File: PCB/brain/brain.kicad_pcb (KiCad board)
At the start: 2 copper layers, 217 parts, among them J1 Screw_Terminal_01x02, J10 Conn_01x12, J11 Conn_01x04, J12 BAT, J2 Conn_01x04, J3 RJ45_Hanrun_HR911105A_Horizon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, J4 Conn_01x04, J5 Conn_01x04, J6 Conn_01x04, J7 Conn_01x06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

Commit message: start pcb routing
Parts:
- moved R51 445.0 mm to (-243.4, 328.6)
- moved R56 439.2 mm to (-242.8, 332.0), turned to -90 degrees
- moved R57 439.0 mm to (-244.3, 332.0), turned to -90 degrees
- moved C84 423.7 mm to (-243.4, 327.0), turned to 180 degrees
- moved J10 422.9 mm to (-324.7, 245.8)
- moved RV1 419.0 mm to (-237.5, 328.7), turned to -90 degrees
- moved C87 416.0 mm to (-238.8, 325.2), turned to -135 degrees
- moved JP3 413.6 mm to (-249.5, 329.7), turned to 90 degrees
- moved R46 412.3 mm to (-208.3, 308.4)
- moved R47 412.3 mm to (-208.3, 311.0)
- moved R48 412.3 mm to (-208.3, 313.5)
- moved R49 412.3 mm to (-208.3, 316.0)
- moved R50 412.3 mm to (-208.3, 318.5)
- moved C88 411.9 mm to (-235.8, 324.8), turned to 90 degrees
- moved JP2 411.0 mm to (-260.0, 321.3), turned to 180 degrees
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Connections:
- C16 pad 2: PMODE0 -> +3.3V
- C57 pad 2: PMODE0 -> +3.3V
- C58 pad 2: PMODE0 -> +3.3V
- C61 pad 2: PMODE0 -> +3.3V
- C62 pad 2: PMODE0 -> +3.3V
- C8 pad 2: PMODE0 -> +3.3V
- C81 pad 2: PMODE0 -> +3.3V
- C82 pad 2: PMODE0 -> +3.3V
- C87 pad 1: PMODE0 -> +3.3V
- C88 pad 2: PMODE0 -> +3.3V
- C89 pad 2: PMODE0 -> +3.3V
- D3 pad 2: PMODE0 -> +3.3V
- FB3 pad 1: PMODE0 -> +3.3V
- J10 pad 4: PMODE0 -> +3.3V
- J3 pad 12: PMODE0 -> +3.3V
- J3 pad 9: PMODE0 -> +3.3V
- J8 pad 2: PMODE0 -> +3.3V
- J8 pad 3: PMODE0 -> +3.3V
- J9 pad 1: OA1 -> OA2
- J9 pad 2: OA2 -> OA1
- JP1 pad 1: PMODE0 -> +3.3V
- JP3 pad 1: PMODE0 -> +3.3V
- JP4 pad 1: PMODE0 -> +3.3V
- L4 pad 2: PMODE0 -> +3.3V
- R12 pad 2: PMODE0 -> +3.3V
- R13 pad 2: PMODE0 -> +3.3V
- R25 pad 1: PMODE0 -> +3.3V
- R29 pad 2: PMODE0 -> +3.3V
- R4 pad 1: PMODE0 -> +3.3V
- R48 pad 1: PMODE0 -> +3.3V
- R52 pad 1: PMODE0 -> +3.3V
- R53 pad 1: PMODE0 -> +3.3V
- R54 pad 1: PMODE0 -> +3.3V
- R55 pad 1: PMODE0 -> +3.3V
- U1 pad 2: PMODE0 -> +3.3V
- U10 pad 3: PMODE0 -> +3.3V
- U14 pad 1: PMODE0 -> +3.3V
- U2 pad 15: PMODE0 -> +3.3V
- U3 pad 28: PMODE0 -> +3.3V
- U3 pad 43: PMODE0 -> PMODE2
- U3 pad 44: PMODE0 -> PMODE1
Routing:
- net GND: track 0.00 -> 112.1 mm, vias 0 -> 7
- net Net-(BT1--): track 0.00 -> 40.2 mm, vias 0 -> 1
- net VS: track 0.00 -> 35.6 mm, vias 0 -> 3
- net +3.3V: track 0.00 -> 34.2 mm, vias 0 -> 4
- net +5V: track 0.00 -> 25.6 mm, vias 0 -> 2
- net +BATT: track 0.00 -> 23.5 mm
- net Net-(BT2--): track 0.00 -> 22.3 mm
- net OA2: track 0.00 -> 12.6 mm
- net OB2: track 0.00 -> 12.6 mm
- net OB1: track 0.00 -> 11.4 mm
- net OA1: track 0.00 -> 11.4 mm
- net Net-(Q1-D): track 0.00 -> 8.29 mm, vias 0 -> 19
- net Net-(Q1-G): track 0.00 -> 8.29 mm, vias 0 -> 2
- net MS1: track 0.00 -> 7.01 mm
- net MS2: track 0.00 -> 6.67 mm, vias 0 -> 2
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
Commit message: TMC2209 done
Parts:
- moved J10 113.9 mm to (-256.6, 337.0), turned to 90 degrees
- moved D11 55.2 mm to (-233.8, 315.8), turned to 180 degrees
- moved D10 49.1 mm to (-236.8, 319.0), turned to 180 degrees
- moved D9 48.1 mm to (-236.8, 317.4)
- moved R46 43.6 mm to (-249.8, 321.6), turned to -90 degrees
- moved C85 40.4 mm to (-258.0, 319.6), turned to -90 degrees
- moved C80 37.5 mm to (-256.5, 319.6), turned to -90 degrees
- moved R47 28.7 mm to (-236.8, 314.2), turned to 180 degrees
- moved R50 28.7 mm to (-236.8, 315.8), turned to 180 degrees
- moved C79 28.5 mm to (-246.8, 322.4), turned to -90 degrees
- moved C83 28.1 mm to (-247.2, 325.0)
- moved R48 25.8 mm to (-233.8, 317.4), turned to 180 degrees
- moved R49 25.5 mm to (-233.6, 319.0)
- moved JP2 1.40 mm to (-261.4, 321.3)
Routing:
- net GND: track 112.1 -> 142.1 mm, vias 7 -> 9
- net STEP: track 1.42 -> 11.9 mm, vias 1 -> 2
- net VS: track 35.6 -> 44.8 mm
- net +3.3V: track 34.2 -> 42.0 mm
- net Net-(JP3-B): track 0.00 -> 7.56 mm
- net DIR: track 0.00 -> 5.60 mm
- net EN: track 0.00 -> 5.52 mm, vias 0 -> 2
- net VCP: track 0.00 -> 2.61 mm
- net Net-(U2-CPO): track 0.00 -> 1.99 mm
- net Net-(U2-CPI): track 0.00 -> 1.95 mm
- net Net-(D10-K): track 0.00 -> 1.59 mm
- net Net-(D9-A): track 0.00 -> 1.39 mm
- net Net-(D11-A): track 0.00 -> 1.39 mm

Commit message: more pcb routing
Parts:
- added C94: 22uF, Capacitor_SMD:C_0805_2012Metric, F.Cu at (-47.9, 179.5)
- C25, C28, C36, C40, C59, C62, C64, C65, C66, C67, C68, C69, C8, C82, C9: footprint Capacitor_SMD:C_0603_1608Metric -> Capacitor_SMD:C_0402_1005Metric
- U11: footprint easyeda2kicad:SOIC-8_L4.9-W3.9-P1.27-LS6.0-BL-EP-1 -> Package_SO:SOIC-8-1EP_3.9x4.9mm_P1.27mm_EP2.29x3mm_ThermalVias
- moved R59 414.3 mm to (-44.9, 182.0), turned to 180 degrees
- moved U11 410.6 mm to (-38.2, 181.1)
- moved R41 408.9 mm to (-37.8, 163.2)
- moved R40 405.2 mm to (-34.7, 163.2)
- moved R26 395.5 mm to (-32.7, 181.9)
- moved R28 394.7 mm to (-36.9, 185.1), turned to 180 degrees
- moved R27 391.2 mm to (-33.8, 185.1), turned to 180 degrees
- moved C53 390.7 mm to (-43.1, 179.7), turned to -90 degrees
- moved L2 389.3 mm to (-30.2, 172.6), turned to 90 degrees
- moved C48 389.1 mm to (-37.8, 171.6)
- moved C43 388.8 mm to (-37.8, 169.5)
- moved C54 388.5 mm to (-46.1, 179.7), turned to -90 degrees
- moved C42 388.4 mm to (-37.8, 167.4)
- moved C41 387.5 mm to (-44.6, 179.7), turned to -90 degrees
- moved C47 386.7 mm to (-40.5, 177.5), turned to 180 degrees
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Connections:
- net Net-(U9-SW1) renamed /SW1
- net Net-(U9-SW2) renamed /SW2
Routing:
- net GND: track 142.1 -> 235.3 mm
- net 5VHP: track 0.00 -> 38.0 mm, vias 0 -> 2
- net Net-(U11-SW): track 0.00 -> 16.6 mm, vias 0 -> 2
- net AMP_VDD: track 0.00 -> 15.3 mm
- net Net-(C6-Pad1): track 0.00 -> 8.64 mm
- net Net-(C5-Pad1): track 0.00 -> 8.64 mm
- net VSYS: track 4.92 -> 12.9 mm
- net Net-(U11-COMP): track 0.00 -> 4.53 mm
- net 5VHP_EN: track 0.00 -> 3.22 mm, vias 0 -> 1
- net Net-(U4-OUTP): track 0.00 -> 2.92 mm
- net Net-(U4-OUTN): track 0.00 -> 2.92 mm
- net Net-(U11-FB): track 0.00 -> 2.25 mm
- net Net-(U11-SS): track 0.00 -> 2.23 mm
- net Net-(U4-~{SD_MODE}): track 0.00 -> 1.80 mm
- net Net-(U11-BST): track 0.00 -> 1.70 mm
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- added copper zone on F.Cu, net /SW1
- added copper zone on F.Cu, net /SW2

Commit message: start component placing on pcb
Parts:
- added C95: 10uF, Capacitor_SMD:C_0603_1608Metric, F.Cu at (257.5, 75.0)
- added C96: 0.1uF, Capacitor_SMD:C_0402_1005Metric, F.Cu at (257.2, 76.5)
- added MK1: ICS-43434, Sensor_Audio:InvenSense_ICS-43434-6_3.5x2.65mm, F.Cu at (254.5, 77.9)
- C30, C31, C32: moved to B.Cu
- moved BT1 243.4 mm to (61.8, 52.8), turned to -90 degrees
- moved BT2 240.5 mm to (55.3, 52.8), turned to -90 degrees
- moved J12 233.6 mm to (54.8, 57.8), turned to 0 degrees
- moved C2 227.8 mm to (57.5, 63.0), turned to 180 degrees
- moved C15 227.7 mm to (67.1, 66.8), turned to 0 degrees
- moved C1 226.1 mm to (58.3, 64.6), turned to 180 degrees
- moved R15 224.3 mm to (59.0, 66.2), turned to 180 degrees
- moved U10 223.8 mm to (67.1, 69.8), turned to 180 degrees
- moved R29 222.7 mm to (65.1, 69.8), turned to 90 degrees
- moved R14 221.7 mm to (58.2, 67.8), turned to 0 degrees
- moved U7 218.1 mm to (58.1, 70.5), turned to 0 degrees
- moved R7 216.7 mm to (60.6, 72.5), turned to -90 degrees
- moved C3 214.2 mm to (55.6, 72.5), turned to 90 degrees
- moved Q2 211.2 mm to (60.2, 76.6), turned to -90 degrees
- moved Q1 209.0 mm to (56.1, 76.6), turned to -90 degrees
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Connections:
- net Net-(U9-PMID) renamed /PMID
- C37 pad 2: VSYS -> VBUS
- C38 pad 2: VSYS -> VBUS
- C39 pad 2: VSYS -> VBUS
- C40 pad 2: VSYS -> VBUS
- R25 pad 2: INT -> BQINT
- TP6 pad 1: INT -> BQINT
- U1 pad 24: unconnected-(U1-IO47-Pad24) -> MicDATA
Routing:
- net GND: track 235.3 -> 355.4 mm, vias 9 -> 90
- net VBUS: track 0.00 -> 37.5 mm
- net Net-(BT1--): track 40.2 -> 10.0 mm
- net VSYS: track 12.9 -> 40.5 mm, vias 0 -> 7
- net REGN: track 0.00 -> 20.7 mm, vias 0 -> 4
- net Net-(R1-Pad1): track 0.00 -> 19.3 mm
- net D-: track 0.00 -> 15.7 mm
- net +3.3V: track 42.0 -> 57.1 mm, vias 4 -> 6
- net SDA: track 0.00 -> 15.0 mm, vias 0 -> 3
- net SCL: track 0.00 -> 14.7 mm, vias 0 -> 3
- net D+: track 0.00 -> 14.3 mm
- net CC1: track 0.00 -> 13.2 mm
- net BQINT: track 0.00 -> 12.9 mm
- net /PMID: track 0.00 -> 12.8 mm
- net CC2: track 0.00 -> 12.3 mm
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- added copper zone on B.Cu, net +BATT
- added copper zone on F.Cu, net +BATT
- added copper zone on F.Cu, net 5VHP
- added copper zone on F.Cu, net 5VHP_EN
- added copper zone on B.Cu, net GND
- added copper zone on F.Cu, net GND
- added copper zone on B.Cu, net Net-(BT1--)
- added copper zone on B.Cu, net Net-(BT2--)
- added copper zone on F.Cu, net Net-(BT2--)
- added copper zone on F.Cu, net Net-(U11-BST)
- added copper zone on F.Cu, net Net-(U11-FB)
- added copper zone on F.Cu, net Net-(U11-SW)
- added copper zone on B.Cu, net REGN
- added copper zone on F.Cu, net VBUS
- added copper zone on F.Cu, net VSYS
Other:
- board outline added: 100 x 100 mm

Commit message: more pcb
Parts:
- J10: footprint Connector_PinSocket_2.54mm:PinSocket_1x12_P2.54mm_Vertical -> Connector_PinHeader_2.54mm:PinHeader_2x06_P2.54mm_Vertical
- moved JP2 287.9 mm to (101.5, 77.2), turned to 0 degrees
- moved C85 271.4 mm to (88.8, 80.3), turned to 180 degrees
- moved C80 269.4 mm to (88.8, 81.8), turned to 180 degrees
- moved C86 269.1 mm to (94.9, 82.6), turned to 0 degrees
- moved R46 263.5 mm to (89.5, 85.0), turned to 180 degrees
- moved J9 260.1 mm to (102.5, 92.2), turned to 90 degrees
- moved JP3 259.9 mm to (81.4, 85.3), turned to 0 degrees
- moved C79 259.1 mm to (88.7, 88.0), turned to 180 degrees
- moved R45 259.1 mm to (95.0, 90.1), turned to 0 degrees
- moved J10 258.9 mm to (67.3, 82.7), turned to 0 degrees
- moved C83 258.6 mm to (86.1, 87.6), turned to -90 degrees
- moved U2 253.6 mm to (88.9, 92.2), turned to -90 degrees
- moved R44 253.4 mm to (95.0, 94.4), turned to 0 degrees
- moved C84 252.6 mm to (84.1, 91.4), turned to 90 degrees
- moved R51 252.0 mm to (82.5, 91.4), turned to -90 degrees
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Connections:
- J10 pad 10: EN -> TmcEN
- R46 pad 1: EN -> TmcEN
- U1 pad 11: EN -> TmcEN
- U2 pad 2: EN -> TmcEN
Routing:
- net +3.3V: track 57.1 -> 80.4 mm, vias 6 -> 22
- net VS: track 44.8 -> 27.8 mm, vias 3 -> 2
- net TmcEN: track 0.00 -> 7.50 mm, vias 0 -> 3
- net EN: track 17.1 -> 11.6 mm, vias 2 -> 0
- net GND: track 355.4 -> 351.3 mm, vias 90 -> 134
- net SDA: track 15.0 -> 18.2 mm
- net RX1: track 0.00 -> 2.31 mm, vias 0 -> 1
- net BQINT: track 12.9 -> 15.0 mm, vias 0 -> 1
- net STEP: track 11.9 -> 13.9 mm, vias 2 -> 3
- net RSTn: track 0.00 -> 1.98 mm, vias 0 -> 1
- net DIR: track 5.60 -> 7.57 mm, vias 0 -> 1
- net CE: track 10.5 -> 12.4 mm, vias 2 -> 3
- net TX1: track 0.00 -> 1.88 mm, vias 0 -> 1
- net SCL: track 14.7 -> 16.6 mm
- net +5V: vias 2 -> 15
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- added copper zone on B.Cu, net +3.3V
- added copper zone on F.Cu, net +3.3V
- added copper zone on B.Cu, net +5V
- added copper zone on F.Cu, net +5V
- added copper zone on F.Cu, net OB2
- added copper zone on B.Cu, net VBUS
- added copper zone on F.Cu, net VS
- added copper zone on B.Cu, net VSYS
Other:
- outline, holes or cut-outs redrawn

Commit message: more pcb
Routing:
- net DIR: track 7.57 -> 52.6 mm, vias 1 -> 2
- net TmcEN: track 7.50 -> 41.8 mm, vias 3 -> 4
- net STEP: track 13.9 -> 46.8 mm
- net DIAG: track 1.74 -> 25.7 mm, vias 1 -> 2
- net VS: track 27.8 -> 47.5 mm, vias 2 -> 3
- net UART: track 2.84 -> 21.2 mm, vias 1 -> 2
- net INDEX: track 4.10 -> 21.6 mm, vias 1 -> 2
- net MS2: track 6.67 -> 20.7 mm
- net +3.3V: track 80.4 -> 91.3 mm
- net MS1: track 7.01 -> 17.9 mm
- net GND: track 351.3 -> 352.6 mm, vias 134 -> 135
- added copper zone on F.Cu, net OA1
- added copper zone on F.Cu, net OA2
- added copper zone on F.Cu, net OB1

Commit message: moar pcb
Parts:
- added J13: Conn_01x05, Connector_JST:JST_XH_B5B-XH-A_1x05_P2.50mm_Vertical, F.Cu at (53.5, 99.0)
- added J14: Conn_01x02, Connector_PinSocket_2.54mm:PinSocket_1x02_P2.54mm_Vertical, F.Cu at (84.0, 110.0)
- moved C95 199.2 mm to (58.9, 91.0), turned to 90 degrees
- moved C96 197.4 mm to (60.4, 91.3), turned to 90 degrees
- moved MK1 193.3 mm to (61.9, 94.0), turned to 90 degrees
- moved LS1 159.4 mm to (115.6, 92.5), turned to 0 degrees
- moved JP1 154.7 mm to (109.6, 76.3), turned to 0 degrees
- moved C6 154.3 mm to (115.3, 85.8), turned to 180 degrees
- moved C60 152.1 mm to (112.6, 78.1), turned to 90 degrees
- moved FB1 151.5 mm to (116.1, 83.3), turned to -90 degrees
- moved C5 150.8 mm to (118.3, 85.8), turned to 0 degrees
- moved C59 150.3 mm to (114.1, 78.1), turned to 90 degrees
- moved FB2 149.7 mm to (117.6, 83.3), turned to -90 degrees
- moved U4 146.5 mm to (117.3, 78.4), turned to -90 degrees
- moved R30 144.6 mm to (116.6, 74.3), turned to 90 degrees
- moved C10 104.4 mm to (102.5, 43.0), turned to -90 degrees
- moved J2 95.6 mm to (109.0, 46.8), turned to 90 degrees
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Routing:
- net GND: track 352.6 -> 371.2 mm, vias 135 -> 151
- net BCLK: track 0.00 -> 11.8 mm
- net LRCLK: track 0.00 -> 7.69 mm
- net MicDATA: track 0.00 -> 7.02 mm
- net AMP_VDD: track 15.3 -> 21.0 mm
- net RX0: track 0.00 -> 5.55 mm
- net TX0: track 0.00 -> 5.48 mm
- net Net-(J11-Pin_1): track 0.00 -> 5.26 mm
- net +3.3V: track 91.3 -> 92.6 mm, vias 22 -> 24
- net VSYS: vias 17 -> 26
- net +5V: vias 15 -> 23
- net (no net): vias 0 -> 1
- added copper zone on F.Cu, net AMP_VDD
- added copper zone on F.Cu, net Net-(C5-Pad1)
- added copper zone on F.Cu, net Net-(C6-Pad1)
- added copper zone on F.Cu, net Net-(U4-OUTN)
- added copper zone on F.Cu, net Net-(U4-OUTP)
- added copper zone on B.Cu, net SCL
- added copper zone on B.Cu, net SDA
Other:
- board size 100 x 100 mm -> 100 x 115 mm

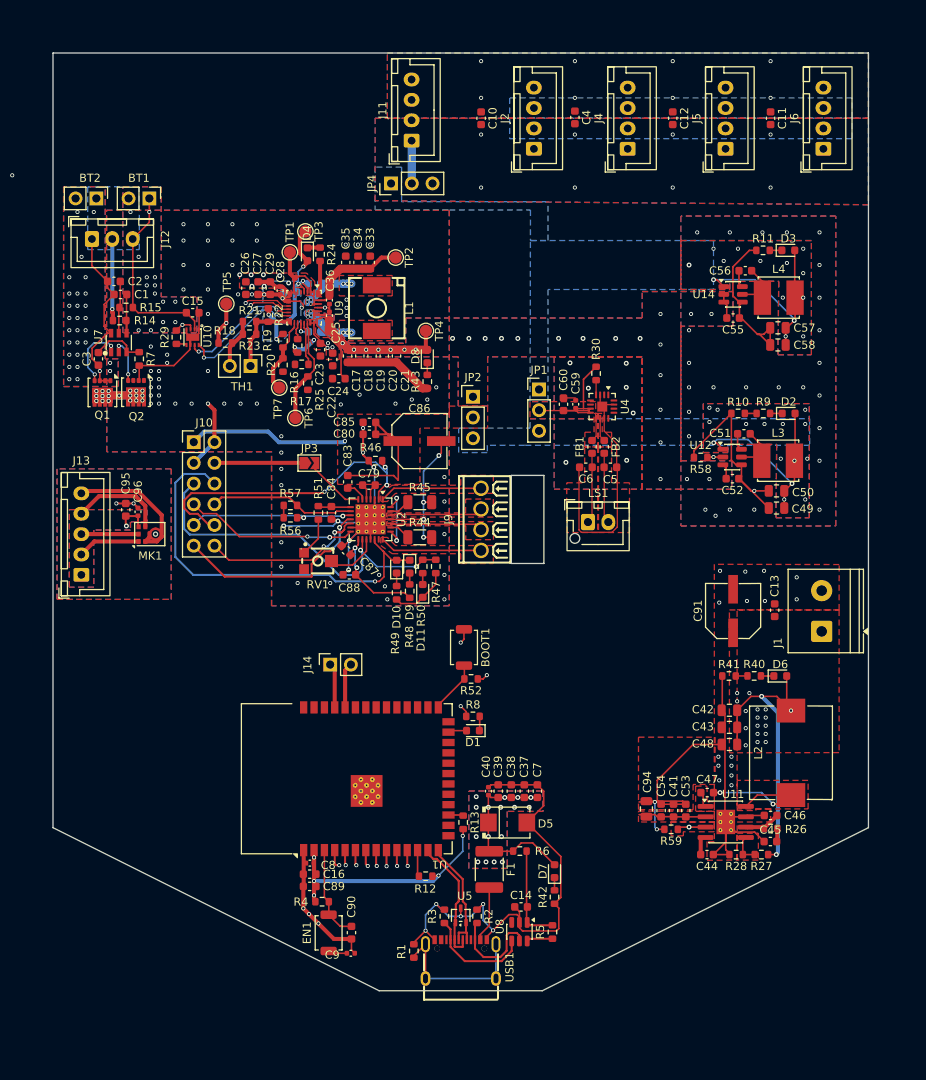
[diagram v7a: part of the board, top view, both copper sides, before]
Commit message: 4layer brain pcb
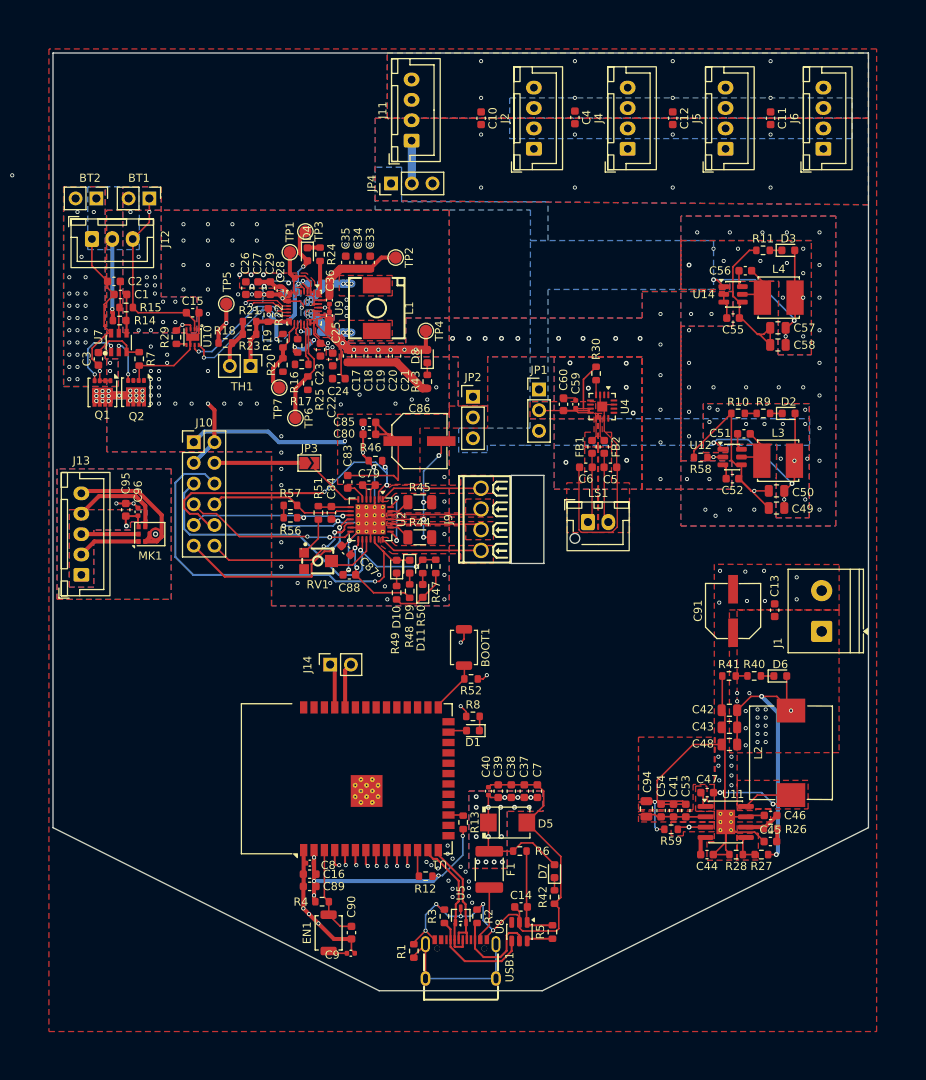
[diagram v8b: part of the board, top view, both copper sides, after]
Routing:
- net GND: vias 151 -> 166
- added copper zone on In1.Cu, net GND
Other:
- copper layers 2 -> 4
